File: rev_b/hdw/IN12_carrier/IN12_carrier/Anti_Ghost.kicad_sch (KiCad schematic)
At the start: 17 parts

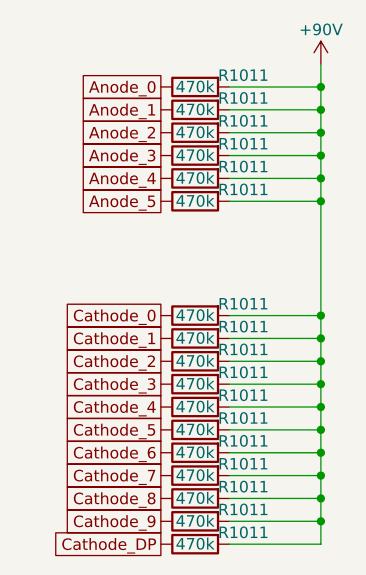
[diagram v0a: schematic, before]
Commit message: updated footprints, ran some DRC
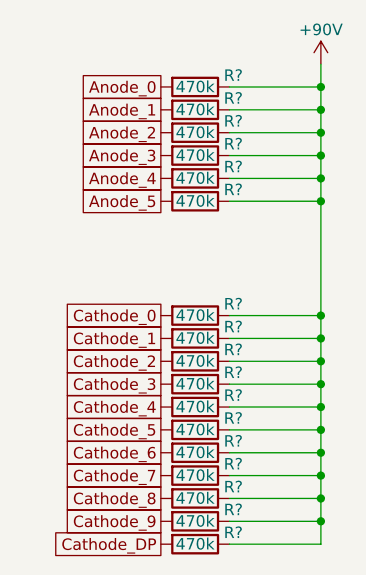
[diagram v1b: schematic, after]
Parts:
- removed R1011 (x17): 470k, Resistors_SMD:R_0402, symbol Nixie-Clock-rescue:R
- added R? (x17): 470k, Resistors_SMD:R_0805, symbol Custom Library:R_Custom
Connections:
- net +90V: now also R?.2, R?.2, R?.2, R?.2, R?.2, R?.2, R?.2, R?.2, R?.2, R?.2, R?.2, R?.2, R?.2, R?.2, R?.2, R?.2, R?.2
- net Anode_0: now also R?.1
- net Anode_1: now also R?.1
- net Anode_2: now also R?.1
- net Anode_3: now also R?.1
- net Anode_4: now also R?.1
- net Anode_5: now also R?.1
- net Cathode_0: now also R?.1
- net Cathode_1: now also R?.1
- net Cathode_2: now also R?.1
- net Cathode_3: now also R?.1
- net Cathode_4: now also R?.1
- net Cathode_5: now also R?.1
- net Cathode_6: now also R?.1
- net Cathode_7: now also R?.1
- net Cathode_8: now also R?.1
- net Cathode_9: now also R?.1
- net Cathode_DP: now also R?.1

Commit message: assigned digikey pns to IN12 carrier board parts
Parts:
- R? (x17): Digi-Key PN PN -> 541-470KCCT-ND
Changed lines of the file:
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@@
       (effects (font (size 1.27 1.27)) hide)
     )
-    (property "Digi-Key PN" "PN" (at 113.03 82.55 0) (show_name)
+    (property "Digi-Key PN" "541-470KCCT-ND" (at 113.03 82.55 0) (show_name)
       (effects (font (size 1.524 1.524)) hide)
     )
@@
       (effects (font (size 1.27 1.27)) hide)
     )
-    (property "Digi-Key PN" "PN" (at 113.03 59.69 0) (show_name)
+    (property "Digi-Key PN" "541-470KCCT-ND" (at 113.03 59.69 0) (show_name)
       (effects (font (size 1.524 1.524)) hide)
     )
@@
       (effects (font (size 1.27 1.27)) hide)
     )
-    (property "Digi-Key PN" "PN" (at 113.03 62.23 0) (show_name)
+    (property "Digi-Key PN" "541-470KCCT-ND" (at 113.03 62.23 0) (show_name)
       (effects (font (size 1.524 1.524)) hide)
     )
@@
       (effects (font (size 1.27 1.27)) hide)
     )
-    (property "Digi-Key PN" "PN" (at 113.03 85.09 0) (show_name)
+    (property "Digi-Key PN" "541-470KCCT-ND" (at 113.03 85.09 0) (show_name)
       (effects (font (size 1.524 1.524)) hide)
     )
@@
       (effects (font (size 1.27 1.27)) hide)
     )
-    (property "Digi-Key PN" "PN" (at 113.03 100.33 0) (show_name)
+    (property "Digi-Key PN" "541-470KCCT-ND" (at 113.03 100.33 0) (show_name)
       (effects (font (size 1.524 1.524)) hide)
     )
@@
       (effects (font (size 1.27 1.27)) hide)
     )
-    (property "Digi-Key PN" "PN" (at 113.03 92.71 0) (show_name)
+    (property "Digi-Key PN" "541-470KCCT-ND" (at 113.03 92.71 0) (show_name)
       (effects (font (size 1.524 1.524)) hide)
     )
@@
       (effects (font (size 1.27 1.27)) hide)
     )
-    (property "Digi-Key PN" "PN" (at 113.03 90.17 0) (show_name)
+    (property "Digi-Key PN" "541-470KCCT-ND" (at 113.03 90.17 0) (show_name)
       (effects (font (size 1.524 1.524)) hide)
     )
@@
       (effects (font (size 1.27 1.27)) hide)
     )
-    (property "Digi-Key PN" "PN" (at 113.03 77.47 0) (show_name)
+    (property "Digi-Key PN" "541-470KCCT-ND" (at 113.03 77.47 0) (show_name)
       (effects (font (size 1.524 1.524)) hide)
     )
@@
       (effects (font (size 1.27 1.27)) hide)
     )
-    (property "Digi-Key PN" "PN" (at 113.03 57.15 0) (show_name)
+    (property "Digi-Key PN" "541-470KCCT-ND" (at 113.03 57.15 0) (show_name)
       (effects (font (size 1.524 1.524)) hide)
     )
@@
       (effects (font (size 1.27 1.27)) hide)
     )
-    (property "Digi-Key PN" "PN" (at 113.03 102.87 0) (show_name)
+    (property "Digi-Key PN" "541-470KCCT-ND" (at 113.03 102.87 0) (show_name)
       (effects (font (size 1.524 1.524)) hide)
     )
@@
       (effects (font (size 1.27 1.27)) hide)
     )
-    (property "Digi-Key PN" "PN" (at 113.03 52.07 0) (show_name)
+    (property "Digi-Key PN" "541-470KCCT-ND" (at 113.03 52.07 0) (show_name)
       (effects (font (size 1.524 1.524)) hide)
     )
@@
       (effects (font (size 1.27 1.27)) hide)
     )
-    (property "Digi-Key PN" "PN" (at 113.03 54.61 0) (show_name)
+    (property "Digi-Key PN" "541-470KCCT-ND" (at 113.03 54.61 0) (show_name)
       (effects (font (size 1.524 1.524)) hide)
     )
@@
       (effects (font (size 1.27 1.27)) hide)
     )
-    (property "Digi-Key PN" "PN" (at 113.03 97.79 0) (show_name)
+    (property "Digi-Key PN" "541-470KCCT-ND" (at 113.03 97.79 0) (show_name)
       (effects (font (size 1.524 1.524)) hide)
     )
@@
       (effects (font (size 1.27 1.27)) hide)
     )
-    (property "Digi-Key PN" "PN" (at 113.03 80.01 0) (show_name)
+    (property "Digi-Key PN" "541-470KCCT-ND" (at 113.03 80.01 0) (show_name)
       (effects (font (size 1.524 1.524)) hide)
     )
@@
       (effects (font (size 1.27 1.27)) hide)
     )
-    (property "Digi-Key PN" "PN" (at 113.03 95.25 0) (show_name)
+    (property "Digi-Key PN" "541-470KCCT-ND" (at 113.03 95.25 0) (show_name)
       (effects (font (size 1.524 1.524)) hide)
     )
@@
       (effects (font (size 1.27 1.27)) hide)
     )
-    (property "Digi-Key PN" "PN" (at 113.03 64.77 0) (show_name)
+    (property "Digi-Key PN" "541-470KCCT-ND" (at 113.03 64.77 0) (show_name)
       (effects (font (size 1.524 1.524)) hide)
     )
@@
       (effects (font (size 1.27 1.27)) hide)
     )
-    (property "Digi-Key PN" "PN" (at 113.03 87.63 0) (show_name)
-      (effects (font (size 1.524 1.524)) hide)
-    )
+    (property "Digi-Key PN" "541-470KCCT-ND" (at 113.03 87.63 0) (show_name)
+      (effects (font (size 1.524 1.524)) hide)
+    )
